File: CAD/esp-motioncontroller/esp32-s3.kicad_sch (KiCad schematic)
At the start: 20 parts, among them J1 Conn_01x06, J7 Screw_Terminal_01x03, U1 ESP32-S3-DevKitC, U15 AMS1117-3.3, U3 XL1509-5.0E1, Y1 32.768khz 3215 12.5pf

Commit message: Feat: 485 single drivers
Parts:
- removed C1, C4: 20pf, Resistor_SMD:R_0603_1608Metric, symbol Library:C
- removed J7: Screw_Terminal_01x03, TerminalBlock_Phoenix:TerminalBlock_Phoenix_PT-1,5-3-3.5-H_1x03_P3.50mm_Horizontal, symbol Connector:Screw_Terminal_01x03
- removed Y1: 32.768khz 3215 12.5pf, Crystal:Crystal_SMD_3215-2Pin_3.2x1.5mm, symbol Library:Crystal
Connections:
- net VDC: now reaches D3.2 (A)

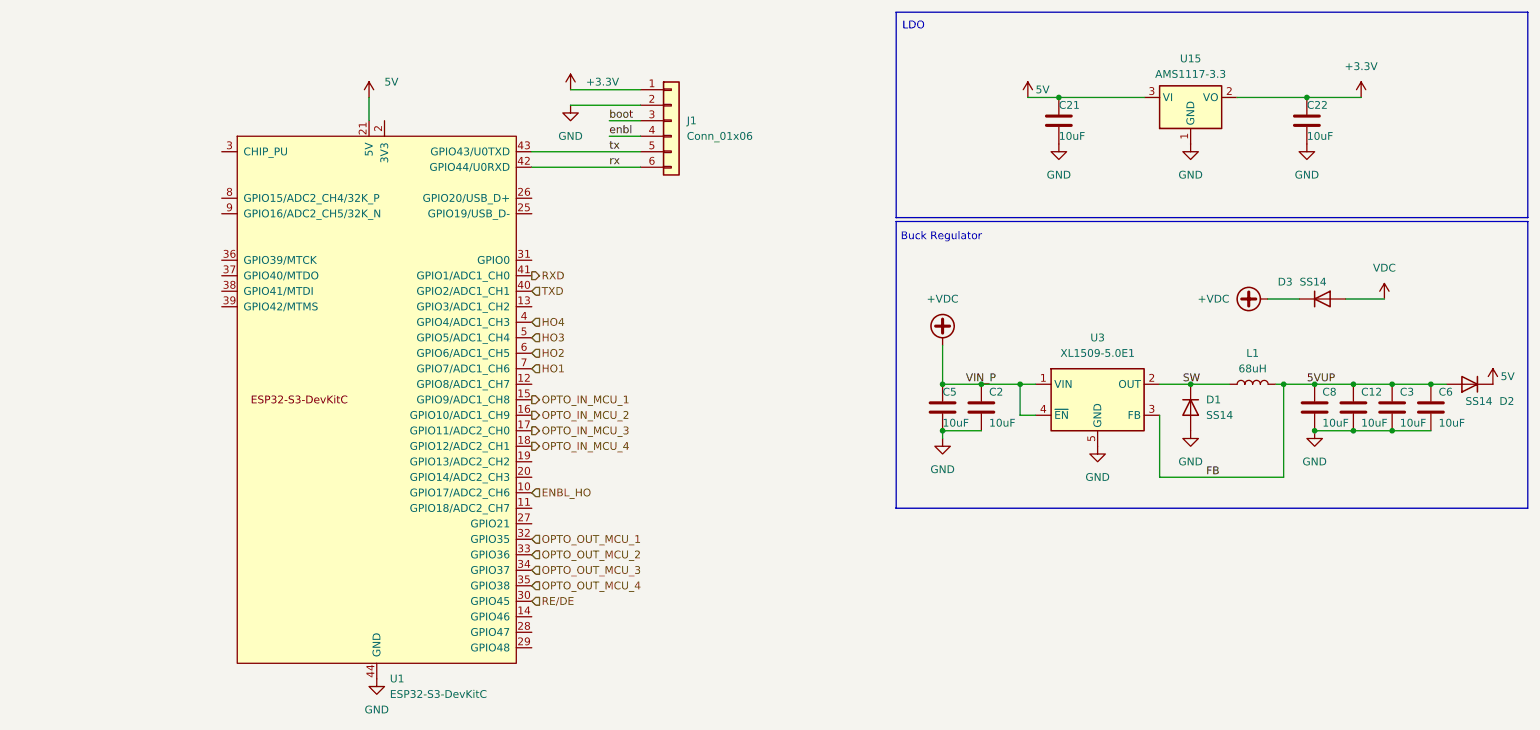
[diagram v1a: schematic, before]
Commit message: Feat: Allmost complete sepdriver
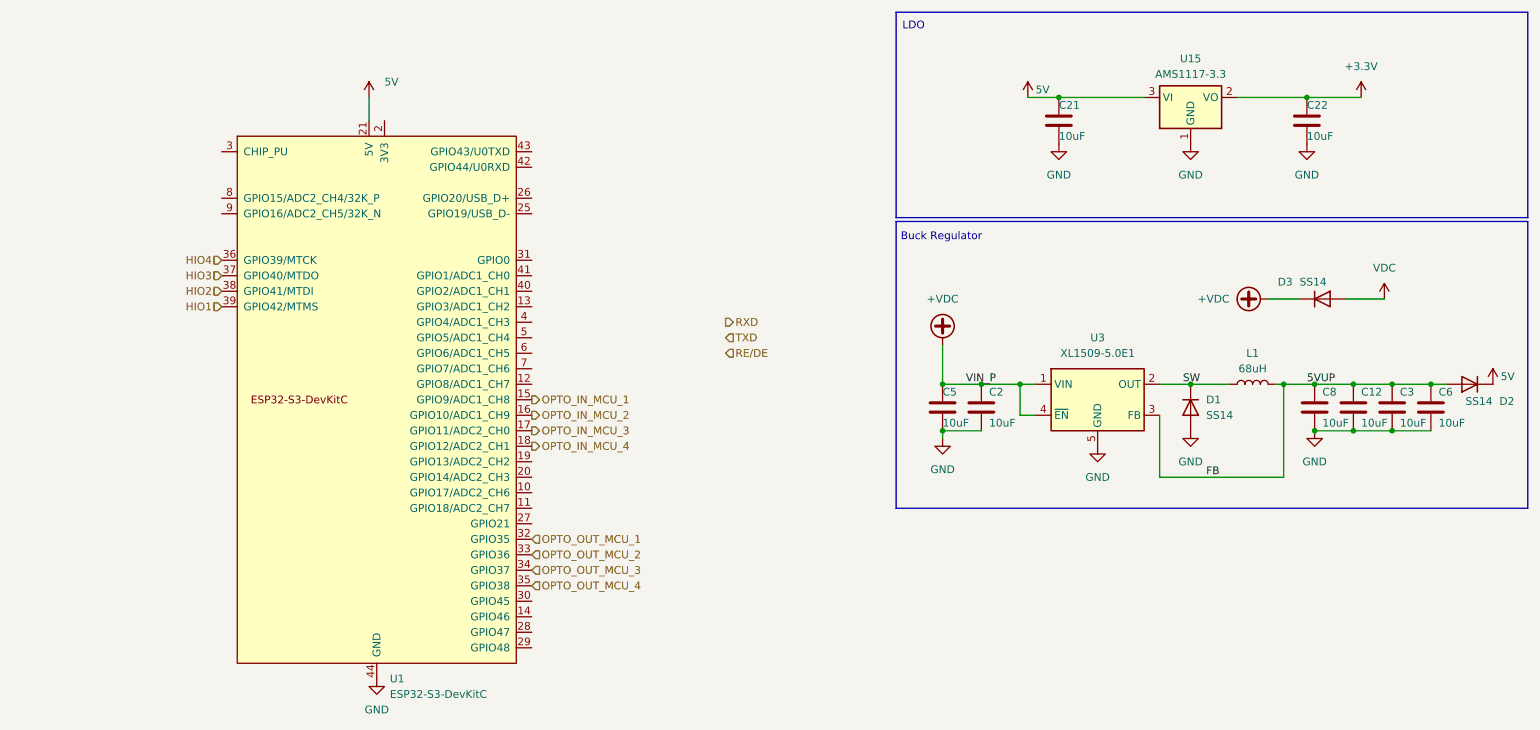
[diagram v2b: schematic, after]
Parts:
- removed J1: Conn_01x06, Connector_PinHeader_2.54mm:PinHeader_1x06_P2.54mm_Vertical, symbol Connector_Generic:Conn_01x06
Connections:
- net RE/DE: no longer U1.30 (GPIO45)
- net RXD: no longer U1.41 (GPIO1/ADC1_CH0)
- net TXD: no longer U1.40 (GPIO2/ADC1_CH1)
- net HIO4: now reaches U1.36 (GPIO39/MTCK)
- net HIO3: now reaches U1.37 (GPIO40/MTDO)
- net HIO2: now reaches U1.38 (GPIO41/MTDI)
- net HIO1: now reaches U1.39 (GPIO42/MTMS)
- net ENBL_HO: no longer names the net of U1.10 (GPIO17/ADC2_CH6)
- net HO1: no longer names the net of U1.7 (GPIO7/ADC1_CH6)
- net HO2: no longer names the net of U1.6 (GPIO6/ADC1_CH5)
- net HO3: no longer names the net of U1.5 (GPIO5/ADC1_CH4)
- net HO4: no longer names the net of U1.4 (GPIO4/ADC1_CH3)
- net rx: no longer names the net of U1.42 (GPIO44/U0RXD)
- net tx: no longer names the net of U1.43 (GPIO43/U0TXD)
